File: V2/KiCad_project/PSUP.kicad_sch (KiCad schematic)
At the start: 36 parts, among them Q201 MMBT3906, Q202 BC846B

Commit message: Fix rotation for JLCPCB
Add `FT Rotation Offset` fields to components that have a wrong
rotation when ordering from JLCPCB.
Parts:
- Q201, Q202: FT Rotation Offset (none) -> 180
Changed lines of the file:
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@@
+			)
+		)
+		(property "FT Rotation Offset" "180"
+			(at 80.01 100.33 0)
+			(effects
+				(font
+					(size 1.27 1.27)
+				)
+				(hide yes)
 			)
 		)
@@
 			)
 		)
+		(property "FT Rotation Offset" "180"
+			(at 69.85 119.38 0)
+			(effects
+				(font
+					(size 1.27 1.27)
+				)
+				(hide yes)
+			)
+		)

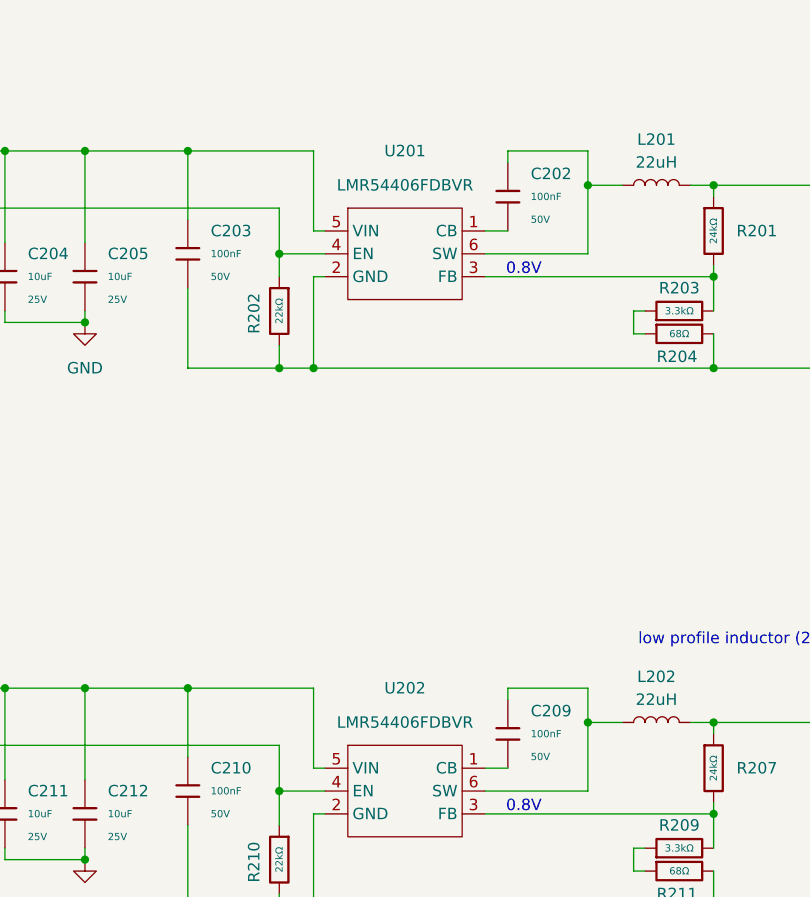
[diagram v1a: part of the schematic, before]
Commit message: Added ordering number to value of U201, U202 and U302 because it did not appear in schematic.pdf and in bom.csv
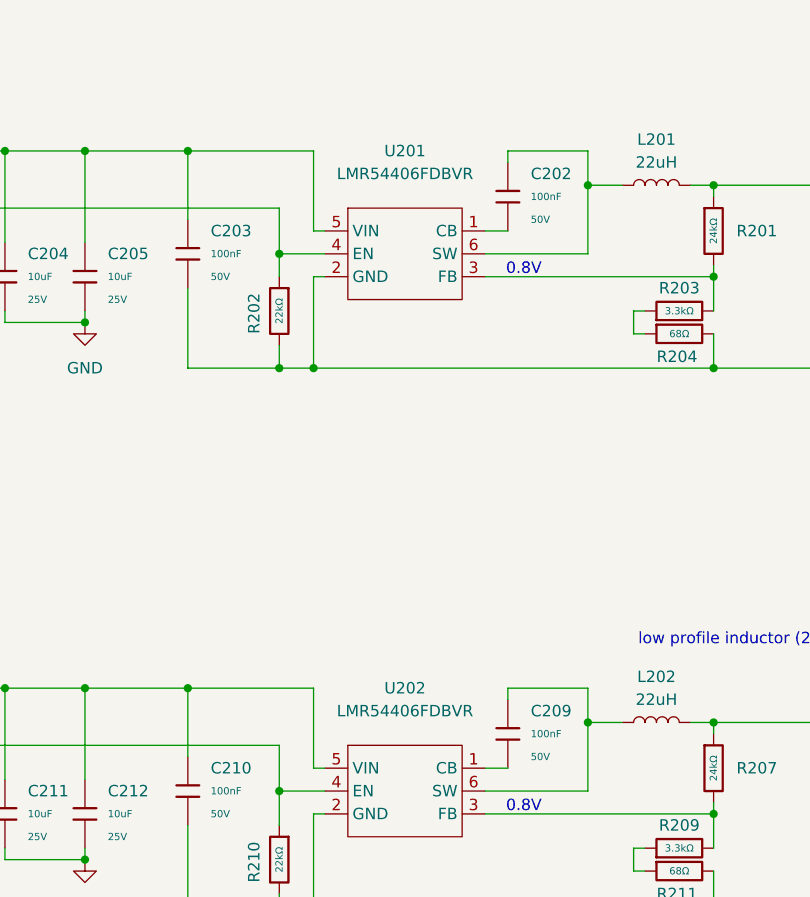
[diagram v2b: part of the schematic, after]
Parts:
- U201, U202: value ~ -> LMR54406FDBVR
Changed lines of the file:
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@@
 			)
 		)
-		(property "Value" "~"
+		(property "Value" "LMR54406FDBVR"
 			(at 158.75 45.72 0)
 			(effects
@@
 					(size 1.27 1.27)
 				)
+				(hide yes)
 			)
 		)
@@
 			)
 		)
-		(property "Value" "~"
+		(property "Value" "LMR54406FDBVR"
 			(at 158.75 105.41 0)
 			(effects
@@
 					(size 1.27 1.27)
 				)
+				(hide yes)
 			)
 		)
